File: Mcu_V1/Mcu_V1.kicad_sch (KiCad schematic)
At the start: 0 parts

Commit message: add com values
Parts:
- added BT1: Battery, symbol Device:Battery
- added C1: 10uF, symbol Device:C
- added C2, C3: 22pF, symbol Device:C
- added C4: 0.1uF, symbol Device:C
- added C5: 100nF, symbol Device:C_Polarized
- added D1, D2: LED, symbol Device:LED
- added H1, H2, H3, H4: MountingHole, symbol Mechanical:MountingHole
- added R1, R2, R6: 10k, symbol Device:R
- added R3, R4: 4.7k, symbol Device:R
- added R5, R7: 330, symbol Device:R
- added U1, U3: 24LC1025, symbol Memory_EEPROM:24LC1025
- added U2: DS1337S_, DS1337S_:SOIC127P600X175-8N, symbol DS1337S_:DS1337S_
- added U4: ATMEGA328P-AU, ATMEGA328P-AU:QFP80P900X900X120-32N, symbol ATMEGA328P-AU:ATMEGA328P-AU
- added Y1: 32.768 KHz, symbol Device:Crystal
- added Y2: 16MHz, symbol Device:Crystal
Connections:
- new net: U4.21 (GND), U4.3 (GND), U4.5 (GND)
- new net: U4.4 (VCC), U4.6 (VCC)
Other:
- added sheet Connectors (Connectors.kicad_sch)
- title: MCU -> ${project_name}

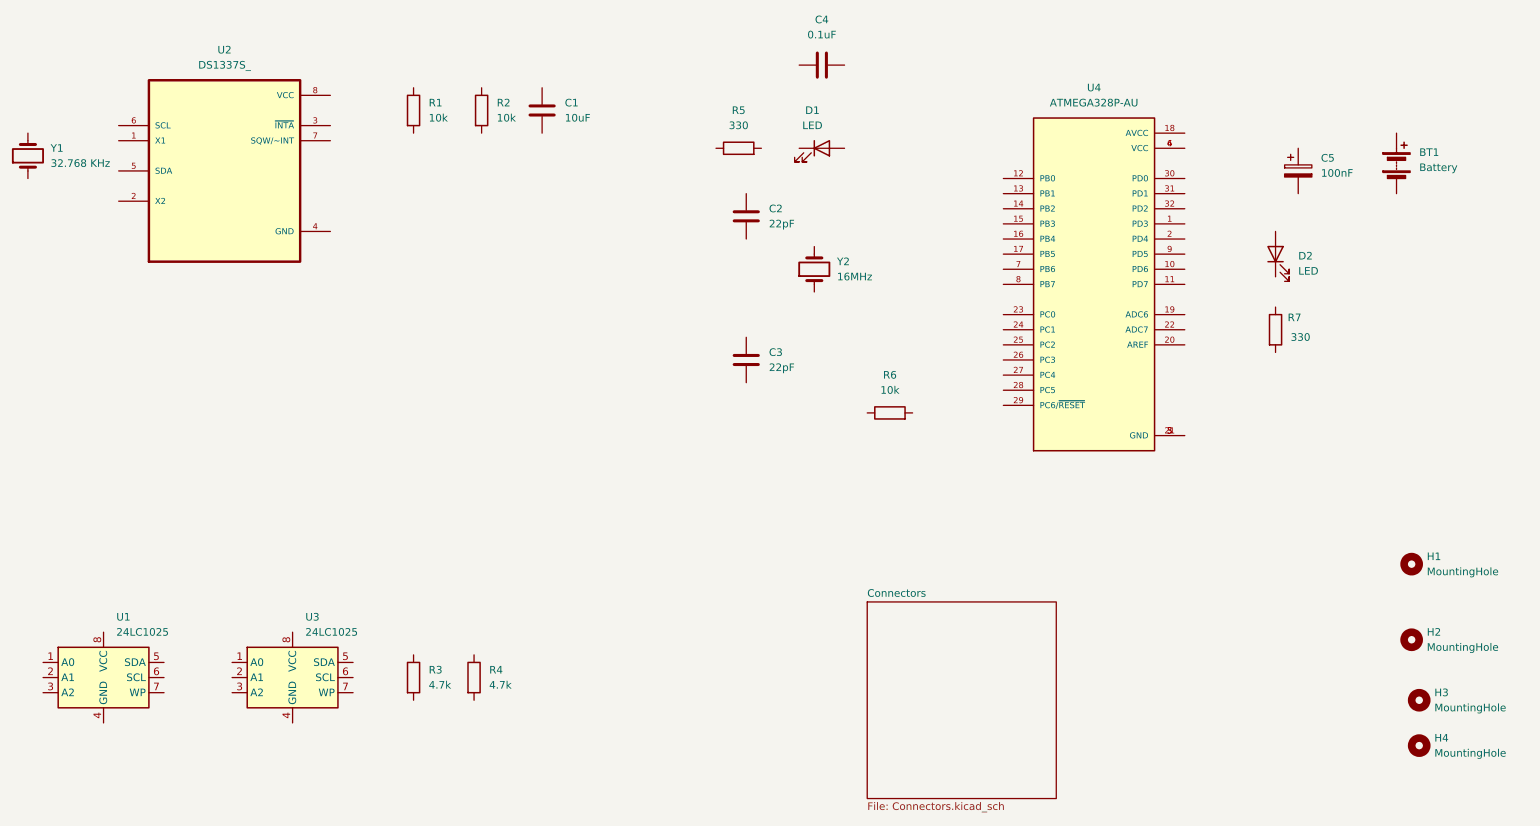
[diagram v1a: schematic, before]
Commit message: wiring done
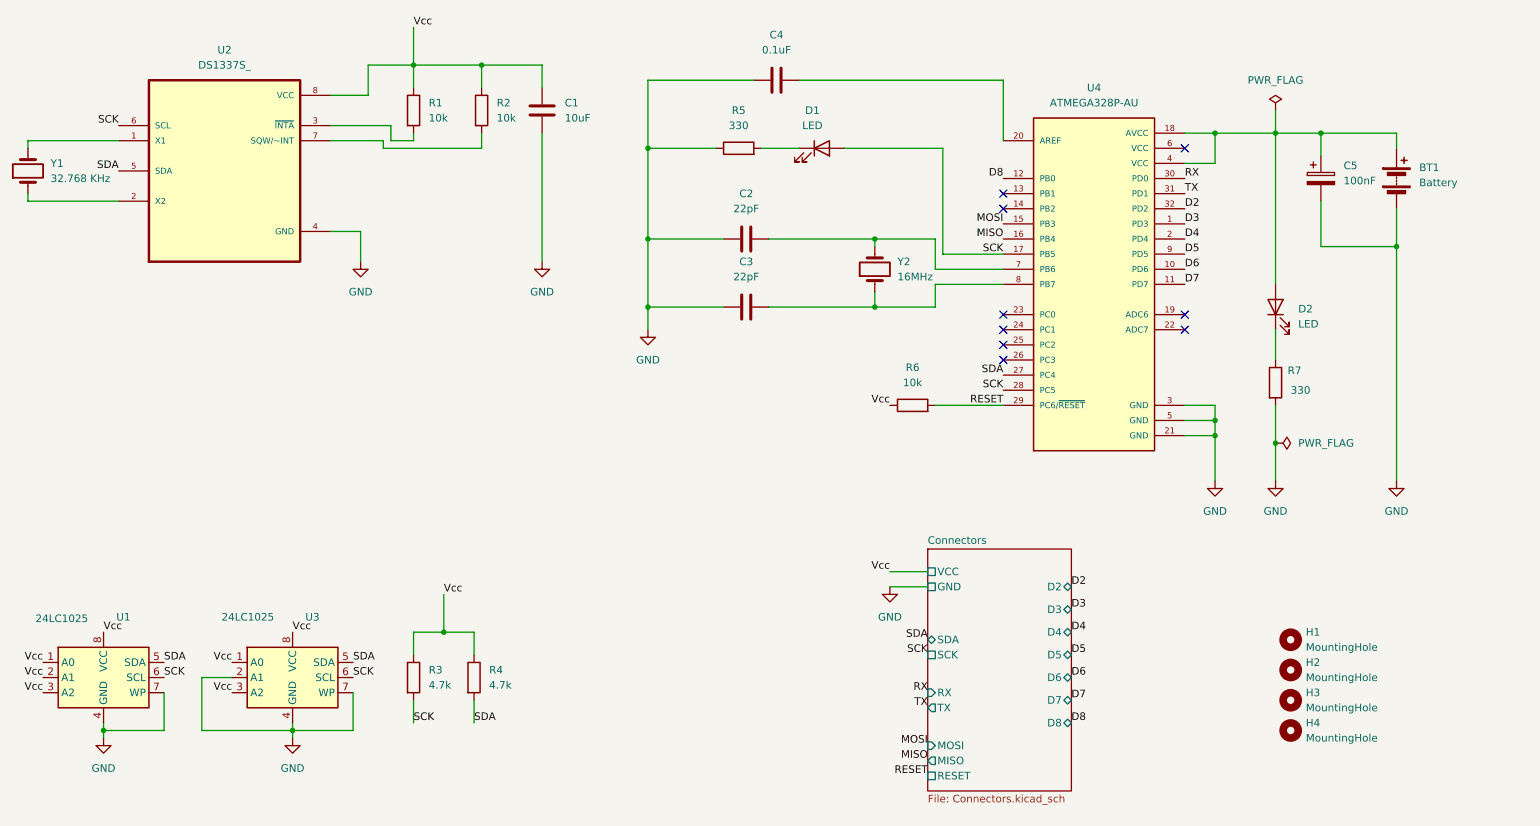
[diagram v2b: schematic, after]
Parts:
- BT1: footprint (none) -> Connector_PinHeader_2.54mm:PinHeader_1x02_P2.54mm_Vertical
- C1, C2, C3, C4, C5: footprint (none) -> Capacitor_SMD:C_0805_2012Metric
- D1, D2: footprint (none) -> LED_SMD:LED_0805_2012Metric
- H1, H2, H3, H4: footprint (none) -> MountingHole:MountingHole_2.1mm
- R1, R2, R3, R4, R5, R6, R7: footprint (none) -> Resistor_SMD:R_0805_2012Metric
- U1, U3: footprint (none) -> Package_SO:SOIC-8_5.3x5.3mm_P1.27mm
- Y1, Y2: footprint (none) -> Crystal:Crystal_SMD_5032-2Pin_5.0x3.2mm_HandSoldering
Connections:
- net Vcc: now reaches R6.1
- net Vcc: now also C1.1, R1.1, R2.1, R3.1, R4.1, U1.1 (A0), U1.2 (A1), U1.3 (A2), U1.8 (VCC), U2.8 (VCC), U3.1 (A0), U3.3 (A2), U3.8 (VCC)
- net RESET: now reaches R6.2
- net RESET: now also U4.29 (PC6/~{RESET})
- net SCK: now reaches R3.2
- net SCK: now also D1.2 (A), U1.6 (SCL), U2.6 (SCL), U3.6 (SCL), U4.17 (PB5), U4.28 (PC5)
- net at BT1.1 (+): now also C5.1, D2.2 (A), U4.18 (AVCC), U4.4 (VCC)
- net GND: now reaches BT1.2 (-)
- net GND: now also C1.2, C2.1, C3.1, C4.1, C5.2, R5.1, R7.2, U1.4 (GND), U1.7 (WP), U2.4 (GND), U3.2 (A1), U3.4 (GND), U3.7 (WP), U4.21 (GND), U4.3 (GND), U4.5 (GND)
- net at R7.1: now also D2.1 (K)
- net SDA: now reaches R4.2
- net SDA: now also U1.5 (SDA), U2.5 (SDA), U3.5 (SDA), U4.27 (PC4)
- net at D1.1 (K): now also R5.2
- net at R1.2: now also U2.3 (~{INTA})
- net at C3.2: now also U4.8 (PB7), Y2.1
- net at R2.2: now also U2.7 (SQW/~INT)
- net D3: now reaches U4.1 (PD3)
- net D6: now reaches U4.10 (PD6)
- net D7: now reaches U4.11 (PD7)
- net D8: now reaches U4.12 (PB0)
- net MOSI: now reaches U4.15 (PB3)
- net MISO: now reaches U4.16 (PB4)
- net D4: now reaches U4.2 (PD4)
- net at U4.20 (AREF): now also C4.2
- net RX: now reaches U4.30 (PD0)
- net TX: now reaches U4.31 (PD1)
- net D2: now reaches U4.32 (PD2)
- net at U4.6 (VCC): no longer U4.4 (VCC)
- net at U4.7 (PB6): now also C2.2, Y2.2
- net D5: now reaches U4.9 (PD5)
- net at U2.1 (X1): now also Y1.2
- net at U2.2 (X2): now also Y1.1
- no-connect marks 0 -> 9
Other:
- sheet Connectors ports: added D2, D3, D4, D5, D6, D7, D8, GND, MISO, MOSI, RESET, RX, SCK, SDA, TX, VCC; removed none
- moved on the sheet: BT1, C2, C3, C4, C5, D2, H1, H2, H3, H4, R6, R7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

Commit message: update
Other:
- sheet Connectors ports: added Vcc; removed VCC
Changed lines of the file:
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@@
 	)
 	(junction
+		(at 50.8 125.73)
+		(diameter 0)
+		(color 0 0 0 0)
+	)
+	(junction
 		(at 82.55 147.32)
 		(diameter 0)
@@
 	(wire
 		(pts
+			(xy 50.8 125.73) (xy 50.8 130.81)
+		)
+		(stroke
+			(width 0)
+			(type default)
+		)
+	)
+	(wire
+		(pts
 			(xy 255.27 66.04) (xy 267.97 66.04)
 		)
@@
 	(wire
 		(pts
+			(xy 53.34 125.73) (xy 50.8 125.73)
+		)
+		(stroke
+			(width 0)
+			(type default)
+		)
+	)
+	(wire
+		(pts
 			(xy 267.97 49.53) (xy 267.97 46.99)
 		)
@@
 	(wire
 		(pts
+			(xy 50.8 123.19) (xy 50.8 125.73)
+		)
+		(stroke
+			(width 0)
+			(type default)
+		)
+	)
+	(wire
+		(pts
 			(xy 113.03 130.81) (xy 113.03 134.62)
 		)
@@
 	)
 	(label "Vcc"
-		(at 50.8 130.81 0)
+		(at 53.34 125.73 0)
 		(effects
 			(font
@@
 	)
 	(symbol
+		(lib_id "power:PWR_FLAG")
+		(at 50.8 123.19 0)
+		(unit 1)
+		(exclude_from_sim no)
+		(in_bom yes)
+		(on_board yes)
+		(dnp no)
+		(fields_autoplaced yes)
+		(property "Reference" "#FLG03"
+			(at 50.8 121.285 0)
+			(effects
+				(font
+					(size 1.27 1.27)
+				)
+				(hide yes)
+			)
+		)
+		(property "Value" "PWR_FLAG"
+			(at 50.8 118.11 0)
+			(effects
+				(font
+					(size 1.27 1.27)
+				)
+			)
+		)
+		(property "Footprint" ""
+			(at 50.8 123.19 0)
+			(effects
+				(font
+					(size 1.27 1.27)
+				)
+				(hide yes)
+			)
+		)
+		(property "Datasheet" "~"
+			(at 50.8 123.19 0)
+			(effects
+				(font
+					(size 1.27 1.27)
+				)
+				(hide yes)
+			)
+		)
+		(property "Description" "Special symbol for telling ERC where power comes from"
+			(at 50.8 123.19 0)
+			(effects
+				(font
+					(size 1.27 1.27)
+				)
+				(hide yes)
+			)
+		)
+		(pin "1"
+		)
+		(instances
+			(project "Mcu_V1"
+				(path "/8a20ec19-5ddc-4fb8-87e4-eca44506b4b3"
+					(reference "#FLG03")
+					(unit 1)
+				)
+			)
+		)
+	)
+	(symbol
 		(lib_id "Device:R")
 		(at 102.87 43.18 0)
@@
 			)
 		)
-		(pin "VCC" passive
-			(at 189.23 120.65 180)
-			(effects
-				(font
-					(size 1.27 1.27)
-				)
-				(justify left)
-			)
-		)
 		(pin "SDA" bidirectional
 			(at 189.23 132.08 180)
@@
 			)
 		)
+		(pin "Vcc" passive
+			(at 189.23 120.65 180)
+			(effects
+				(font
+					(size 1.27 1.27)
+				)
+				(justify left)
+			)
+		)

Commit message: 4 layer done
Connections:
- net Vcc: now also BT1.1 (+), C5.1, D2.2 (A), U4.18 (AVCC), U4.4 (VCC)
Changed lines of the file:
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@@
+	)
+	(label "Vcc"
+		(at 267.97 46.99 180)
+		(effects
+			(font
+				(size 1.27 1.27)
+			)
+			(justify right bottom)
+		)
 	)
 	(label "Vcc"
